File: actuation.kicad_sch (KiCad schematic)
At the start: 21 parts, among them J1 ACTUATION, U1 PCA9615, U2 LP5912-3.3DRV

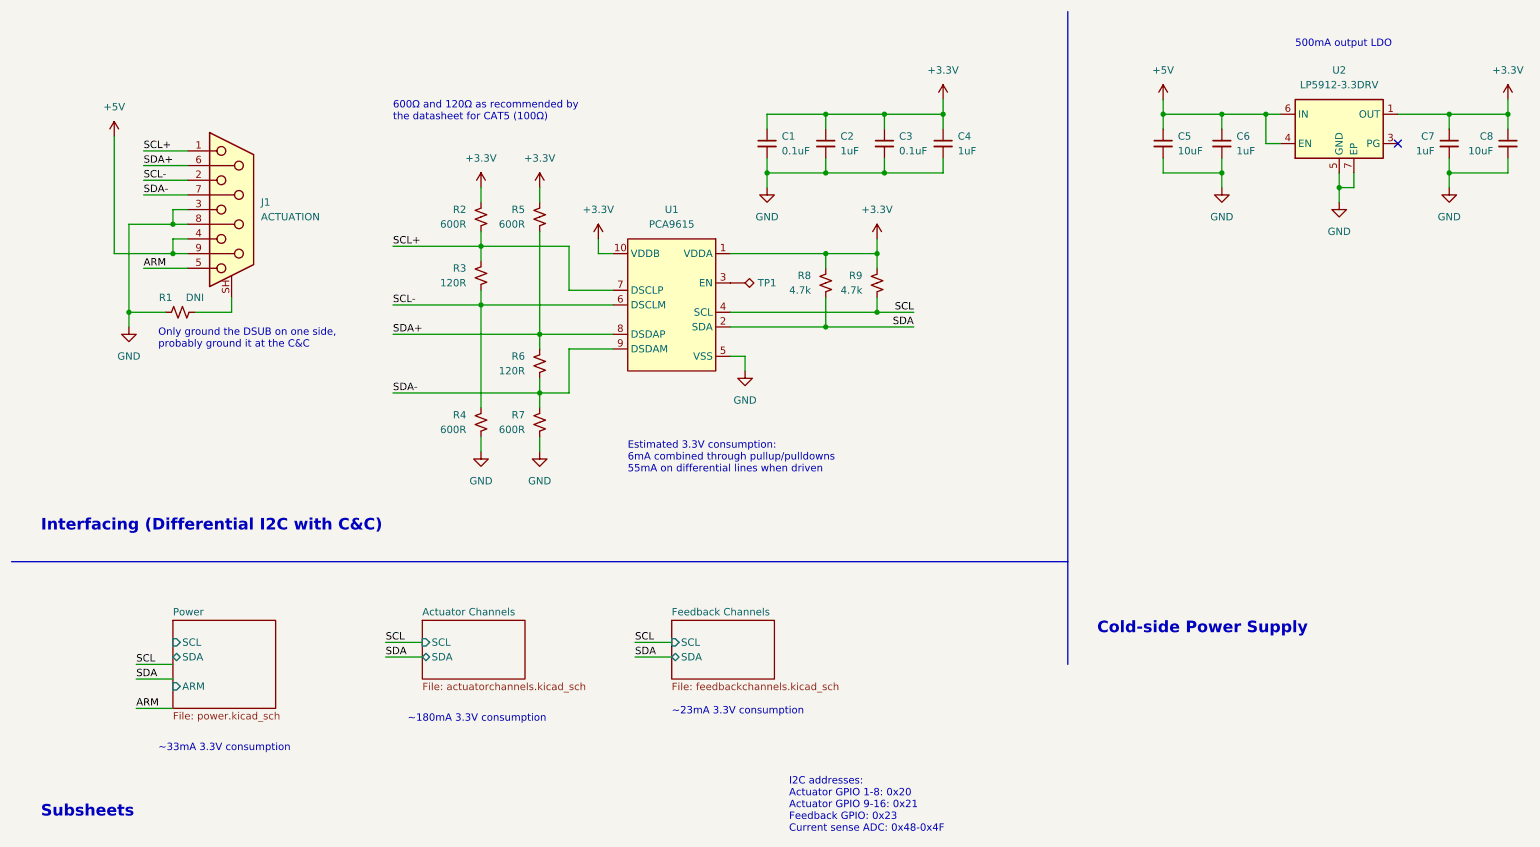
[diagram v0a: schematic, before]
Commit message: labeled chips with their function
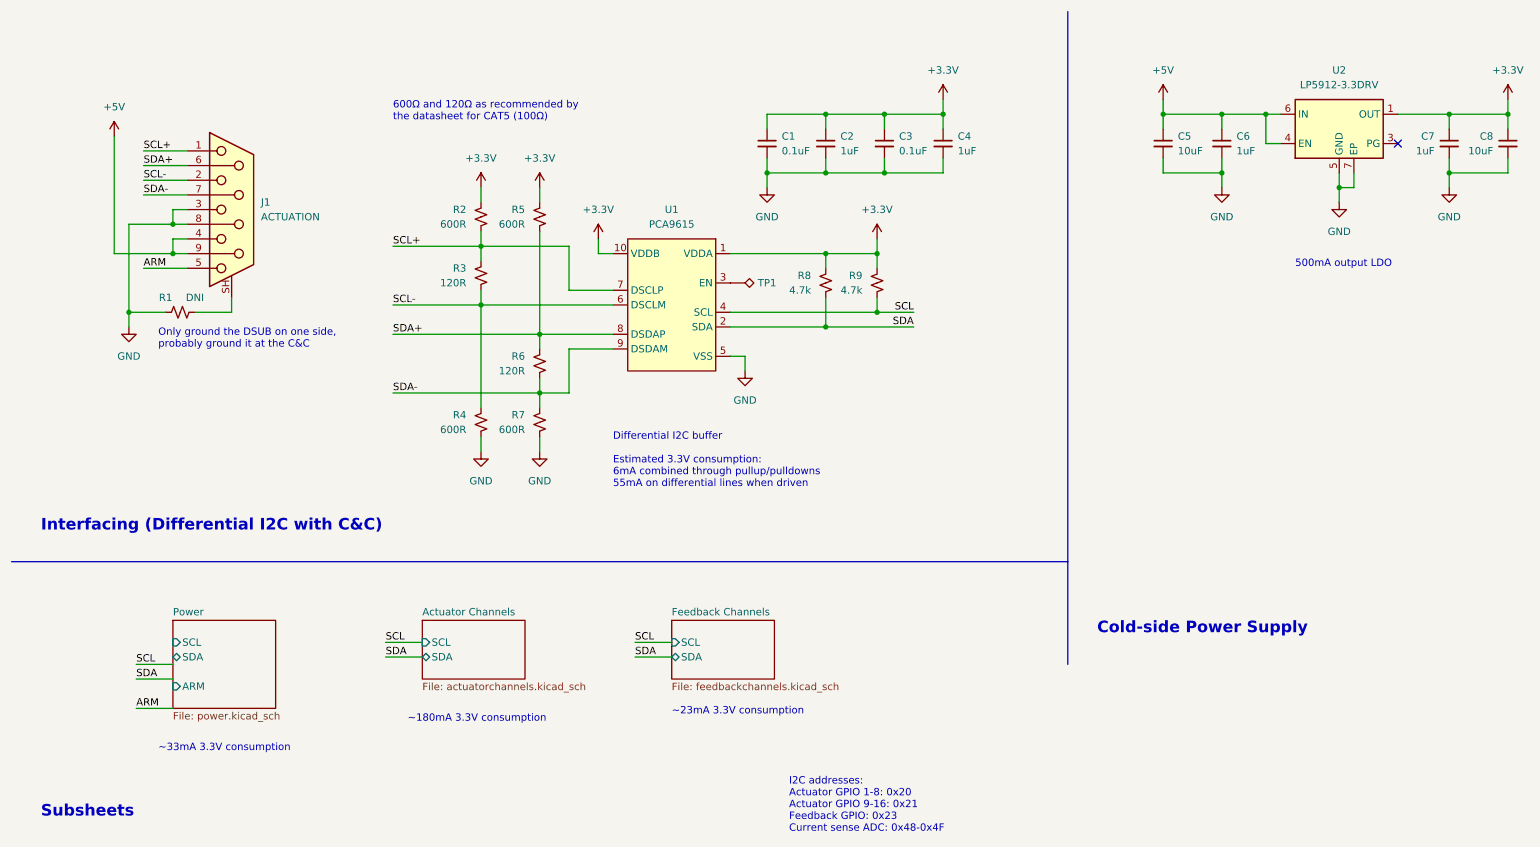
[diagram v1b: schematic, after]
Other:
- note added: "Differential I2C buffer Estimated 3.3V consumption: 6mA combined through pullup/pulldowns 55mA on differential lines when driven"
- note removed: "Estimated 3.3V consumption: 6mA combined through pullup/pulldowns 55mA on differential lines when driven"
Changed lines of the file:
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@@
     (effects (font (size 1.27 1.27)) (justify left bottom))
   )
-  (text "500mA output LDO" (at 234.95 19.05 0)
+  (text "500mA output LDO" (at 234.95 57.15 0)
     (effects (font (size 1.27 1.27)) (justify left bottom))
   )
@@
     (effects (font (size 2 2) bold) (justify left bottom))
   )
-  (text "Estimated 3.3V consumption:\n6mA combined through pullup/pulldowns\n55mA on differential lines when driven"
-    (at 119.38 92.71 0)
+  (text "Differential I2C buffer\n\nEstimated 3.3V consumption:\n6mA combined through pullup/pulldowns\n55mA on differential lines when driven"
+    (at 116.84 95.25 0)
     (effects (font (size 1.27 1.27)) (justify left bottom))
   )

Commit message: Added feedback indicator LED buffer and made changes to notes
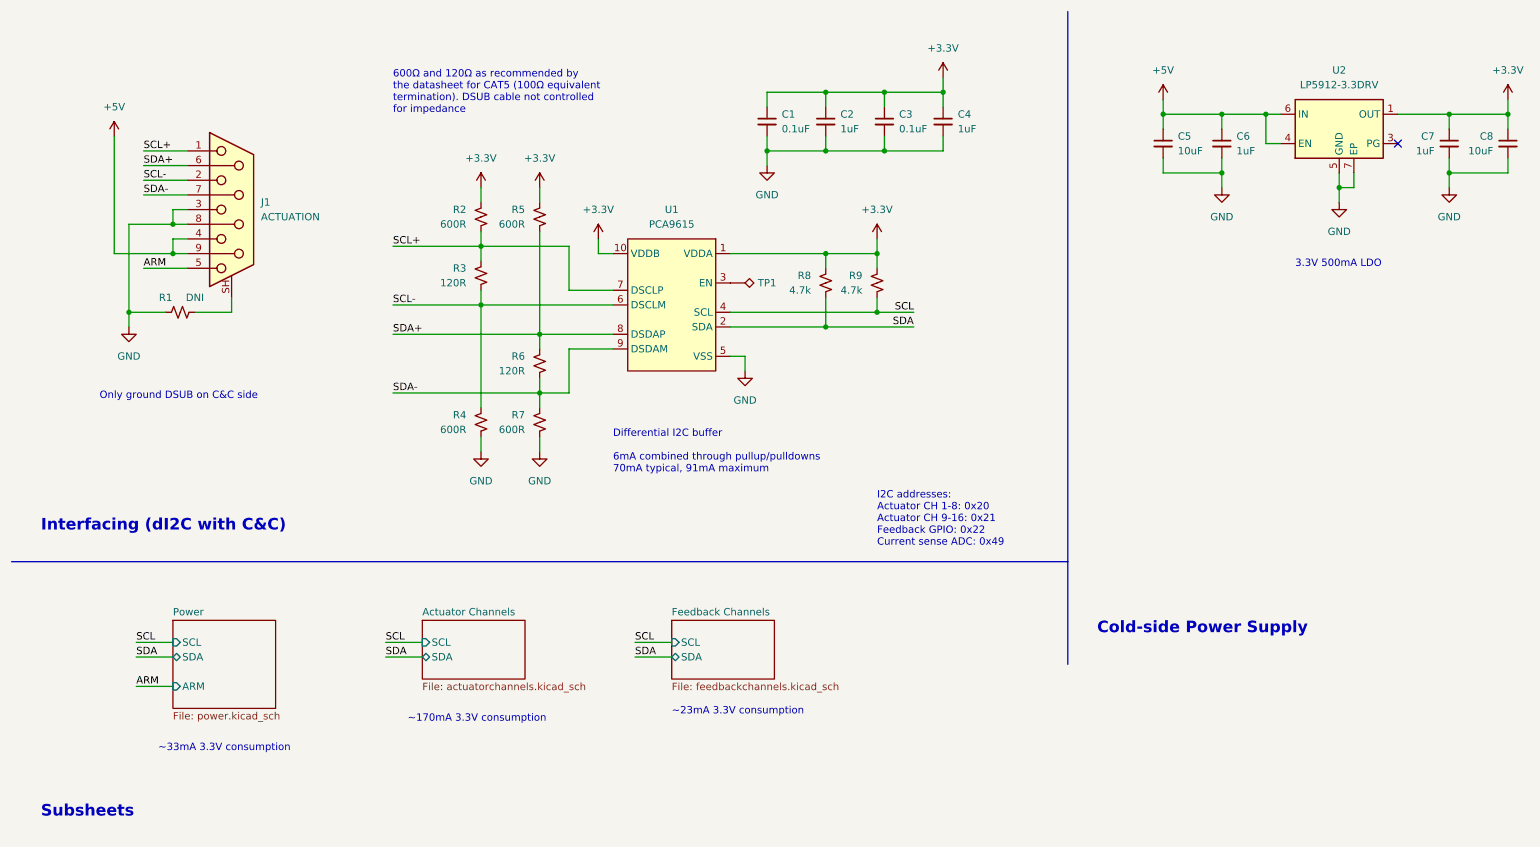
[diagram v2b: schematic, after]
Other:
- note added: "3.3V 500mA LDO"
- note added: "600Ω and 120Ω as recommended by the datasheet for CAT5 (100Ω equivalent termination). DSUB cable not controlled for impedance"
- note added: "Differential I2C buffer 6mA combined through pullup/pulldowns 70mA typical, 91mA maximum"
- note added: "I2C addresses: Actuator CH 1-8: 0x20 Actuator CH 9-16: 0x21 Feedback GPIO: 0x22 Current sense ADC: 0x49"
- note added: "Interfacing (dI2C with C&C)"
- note added: "Only ground DSUB on C&C side"
- note added: "~170mA 3.3V consumption"
- note removed: "500mA output LDO"
- note removed: "600Ω and 120Ω as recommended by the datasheet for CAT5 (100Ω)"
- note removed: "Differential I2C buffer Estimated 3.3V consumption: 6mA combined through pullup/pulldowns 55mA on differential lines when driven"
- note removed: "I2C addresses: Actuator GPIO 1-8: 0x20 Actuator GPIO 9-16: 0x21 Feedback GPIO: 0x23 Current sense ADC: 0x48-0x4F"
- note removed: "Interfacing (Differential I2C with C&C)"
- note removed: "Only ground the DSUB on one side, probably ground it at the C&C"
- note removed: "~180mA 3.3V consumption"
- moved on the sheet: C1, C2, C3, C4

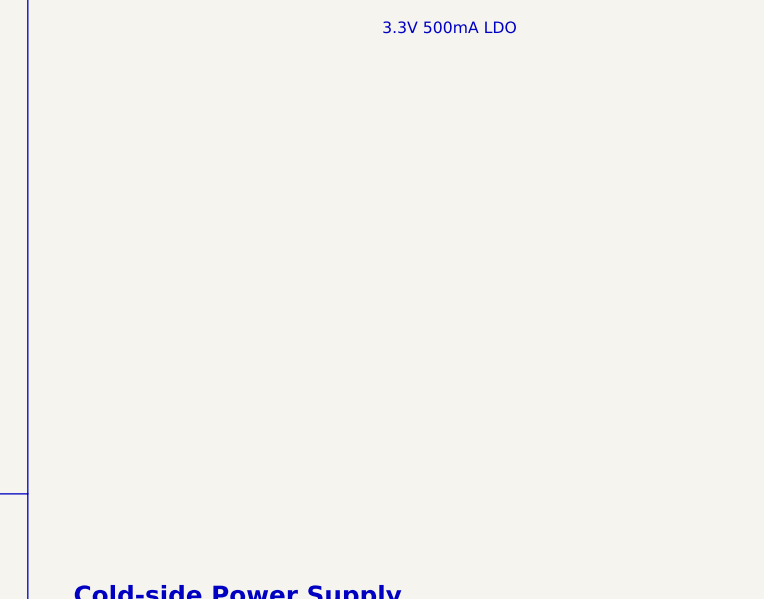
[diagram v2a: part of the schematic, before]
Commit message: Footprints, some part selection, external power outputs
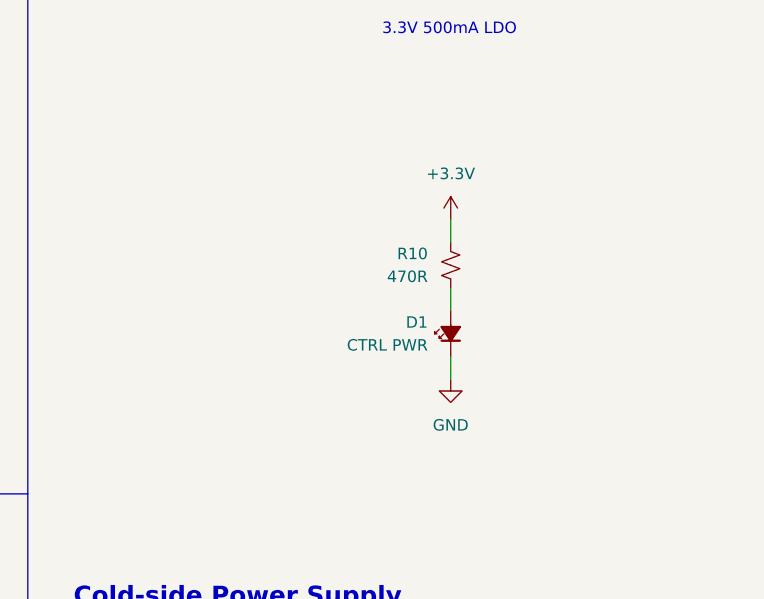
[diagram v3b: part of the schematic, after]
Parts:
- added D1: CTRL PWR, LED_SMD:LED_0603_1608Metric, symbol Device:LED_Small_Filled
- added R10: 470R, Resistor_SMD:R_0603_1608Metric, symbol Device:R_Small_US
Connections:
- net +3.3V: now also R10.1
- net GND: now also D1.1 (K)
- new net: D1.2 (A), R10.2

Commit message: Schematic reorganization
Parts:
- removed C5, C8: 10uF, Capacitor_SMD:C_0805_2012Metric, symbol Device:C_Small
- removed C6, C7: 1uF, Capacitor_SMD:C_0603_1608Metric, symbol Device:C_Small
- removed D1: CTRL PWR, LED_SMD:LED_0603_1608Metric, symbol Device:LED_Small_Filled
- removed R10: 470R, Resistor_SMD:R_0603_1608Metric, symbol Device:R_Small_US
- removed U2: LP5912-3.3DRV, Package_SON:WSON-6-1EP_2x2mm_P0.65mm_EP1x1.6mm_ThermalVias, symbol Regulator_Linear:LP5912-3.3DRV
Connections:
- no-connect marks 1 -> 0
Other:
- note removed: "3.3V 500mA LDO"
- note removed: "Cold-side Power Supply"
- moved on the sheet: C1, C2, C3, C4, J1, R1, R2, R3, R4, R5, R6, R7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
